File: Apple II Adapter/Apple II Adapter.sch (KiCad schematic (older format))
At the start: 20 parts, among them J1 IDC_PORT1, J2 IDC_PORT2, U1 74HCT04, U2 4066

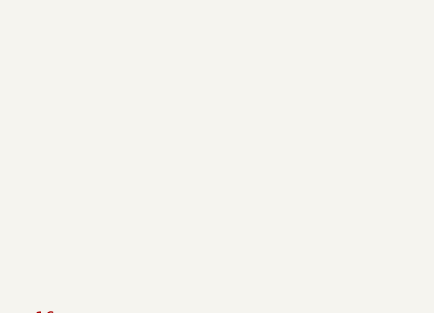
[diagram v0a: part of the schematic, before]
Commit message: Assigned footprints
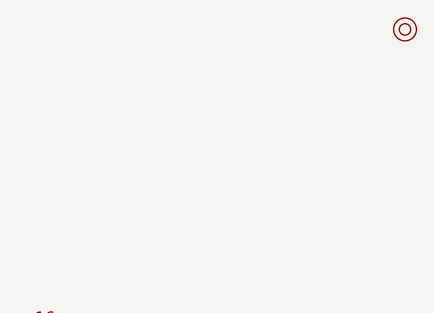
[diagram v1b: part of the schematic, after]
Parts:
- added M1: Mounting, Mounting:M3, symbol mounting:Mounting
- A1: footprint (none) -> Package_DIP:DIP-16_W7.62mm_Socket_LongPads
- C1: footprint (none) -> Capacitor_THT:CP_Radial_D4.0mm_P2.00mm
- J1, J2: footprint (none) -> C64 JoyKEY:IDC_Joystick
- R1, R10, R11, R12, R13, R14, R2, R3, R4, R5, R6, R7, R8, R9: footprint (none) -> Resistor_THT:R_Axial_DIN0207_L6.3mm_D2.5mm_P10.16mm_Horizontal
- U1, U2: footprint (none) -> Package_DIP:DIP-14_W7.62mm_Socket_LongPads
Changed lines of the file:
@@
 F 0 "J1" H 5187 5365 50  0000 C CNN
 F 1 "IDC_PORT1" H 5187 5274 50  0000 C CNN
-F 2 "" H 5200 4625 50  0001 C CNN
+F 2 "C64 JoyKEY:IDC_Joystick" H 5200 4625 50  0001 C CNN
 F 3 "" H 5200 4625 50  0001 C CNN
 	1    5175 4950
@@
 F 0 "J2" H 5187 2565 50  0000 C CNN
 F 1 "IDC_PORT2" H 5187 2474 50  0000 C CNN
-F 2 "" H 5200 1825 50  0001 C CNN
+F 2 "C64 JoyKEY:IDC_Joystick" H 5200 1825 50  0001 C CNN
 F 3 "" H 5200 1825 50  0001 C CNN
 	1    5175 2150
@@
 F 0 "A1" H 9187 2465 50  0000 C CNN
 F 1 "Game_IO" H 9187 2374 50  0000 C CNN
-F 2 "" H 9200 1725 50  0001 C CNN
+F 2 "Package_DIP:DIP-16_W7.62mm_Socket_LongPads" H 9200 1725 50  0001 C CNN
 F 3 "" H 9200 1725 50  0001 C CNN
 	1    9175 2050
@@
 F 0 "U2" H 1700 5527 50  0000 C CNN
 F 1 "4066" H 1700 5436 50  0000 C CNN
-F 2 "" H 1700 5700 50  0001 C CNN
+F 2 "Package_DIP:DIP-14_W7.62mm_Socket_LongPads" H 1700 5700 50  0001 C CNN
 F 3 "http://www.ti.com/lit/ds/symlink/cd4066b.pdf" H 1700 5700 50  0001 C CNN
 	1    1700 5700
@@
 F 0 "U2" H 1700 6777 50  0000 C CNN
 F 1 "4066" H 1700 6686 50  0000 C CNN
-F 2 "" H 1700 6950 50  0001 C CNN
+F 2 "Package_DIP:DIP-14_W7.62mm_Socket_LongPads" H 1700 6950 50  0001 C CNN
 F 3 "http://www.ti.com/lit/ds/symlink/cd4066b.pdf" H 1700 6950 50  0001 C CNN
 	2    1700 6950
@@
 F 0 "U2" H 1700 2727 50  0000 C CNN
 F 1 "4066" H 1700 2636 50  0000 C CNN
-F 2 "" H 1700 2900 50  0001 C CNN
+F 2 "Package_DIP:DIP-14_W7.62mm_Socket_LongPads" H 1700 2900 50  0001 C CNN
 F 3 "http://www.ti.com/lit/ds/symlink/cd4066b.pdf" H 1700 2900 50  0001 C CNN
 	3    1700 2900
@@
 F 0 "U2" H 1700 3977 50  0000 C CNN
 F 1 "4066" H 1700 3886 50  0000 C CNN
-F 2 "" H 1700 4150 50  0001 C CNN
+F 2 "Package_DIP:DIP-14_W7.62mm_Socket_LongPads" H 1700 4150 50  0001 C CNN
 F 3 "http://www.ti.com/lit/ds/symlink/cd4066b.pdf" H 1700 4150 50  0001 C CNN
 	4    1700 4150
@@
 F 0 "U2" H 10580 5696 50  0000 L CNN
 F 1 "4066" H 10580 5605 50  0000 L CNN
-F 2 "" H 10350 5650 50  0001 C CNN
+F 2 "Package_DIP:DIP-14_W7.62mm_Socket_LongPads" H 10350 5650 50  0001 C CNN
 F 3 "http://www.ti.com/lit/ds/symlink/cd4066b.pdf" H 10350 5650 50  0001 C CNN
 	5    10350 5650
@@
 F 0 "U1" H 1325 6892 50  0000 C CNN
 F 1 "74HCT04" H 1325 6801 50  0000 C CNN
-F 2 "" H 1325 6575 50  0001 C CNN
+F 2 "Package_DIP:DIP-14_W7.62mm_Socket_LongPads" H 1325 6575 50  0001 C CNN
 F 3 "https://assets.nexperia.com/documents/data-sheet/74HC_HCT04.pdf" H 1325 6575 50  0001 C CNN
 	1    1325 6575
@@
 F 0 "U1" H 1325 5642 50  0000 C CNN
 F 1 "74HCT04" H 1325 5551 50  0000 C CNN
-F 2 "" H 1325 5325 50  0001 C CNN
+F 2 "Package_DIP:DIP-14_W7.62mm_Socket_LongPads" H 1325 5325 50  0001 C CNN
 F 3 "https://assets.nexperia.com/documents/data-sheet/74HC_HCT04.pdf" H 1325 5325 50  0001 C CNN
 	2    1325 5325
@@
 F 0 "U1" H 7825 6167 50  0000 C CNN
 F 1 "74HCT04" H 7825 6076 50  0000 C CNN
-F 2 "" H 7825 5850 50  0001 C CNN
+F 2 "Package_DIP:DIP-14_W7.62mm_Socket_LongPads" H 7825 5850 50  0001 C CNN
 F 3 "https://assets.nexperia.com/documents/data-sheet/74HC_HCT04.pdf" H 7825 5850 50  0001 C CNN
 	3    7825 5850
@@
 F 0 "U1" H 8325 6167 50  0000 C CNN
 F 1 "74HCT04" H 8325 6076 50  0000 C CNN
-F 2 "" H 8325 5850 50  0001 C CNN
+F 2 "Package_DIP:DIP-14_W7.62mm_Socket_LongPads" H 8325 5850 50  0001 C CNN
 F 3 "https://assets.nexperia.com/documents/data-sheet/74HC_HCT04.pdf" H 8325 5850 50  0001 C CNN
 	4    8325 5850
@@
 F 0 "U1" H 1325 4092 50  0000 C CNN
 F 1 "74HCT04" H 1325 4001 50  0000 C CNN
-F 2 "" H 1325 3775 50  0001 C CNN
+F 2 "Package_DIP:DIP-14_W7.62mm_Socket_LongPads" H 1325 3775 50  0001 C CNN
 F 3 "https://assets.nexperia.com/documents/data-sheet/74HC_HCT04.pdf" H 1325 3775 50  0001 C CNN
 	5    1325 3775
@@
 F 0 "U1" H 1325 2842 50  0000 C CNN
 F 1 "74HCT04" H 1325 2751 50  0000 C CNN
-F 2 "" H 1325 2525 50  0001 C CNN
+F 2 "Package_DIP:DIP-14_W7.62mm_Socket_LongPads" H 1325 2525 50  0001 C CNN
 F 3 "https://assets.nexperia.com/documents/data-sheet/74HC_HCT04.pdf" H 1325 2525 50  0001 C CNN
 	6    1325 2525
@@
 F 0 "U1" H 9730 5696 50  0000 L CNN
 F 1 "74HCT04" H 9730 5605 50  0000 L CNN
-F 2 "" H 9500 5650 50  0001 C CNN
+F 2 "Package_DIP:DIP-14_W7.62mm_Socket_LongPads" H 9500 5650 50  0001 C CNN
 F 3 "https://assets.nexperia.com/documents/data-sheet/74HC_HCT04.pdf" H 9500 5650 50  0001 C CNN
 	7    9500 5650
@@
 F 0 "R11" V 2200 5700 50  0000 C CNN
 F 1 "100k" V 2300 5700 50  0000 C CNN
-F 2 "" V 2230 5700 50  0001 C CNN
+F 2 "Resistor_THT:R_Axial_DIN0207_L6.3mm_D2.5mm_P10.16mm_Horizontal" V 2230 5700 50  0001 C CNN
 F 3 "~" H 2300 5700 50  0001 C CNN
 	1    2300 5700
@@
 F 0 "R12" V 2200 6950 50  0000 C CNN
 F 1 "100k" V 2300 6950 50  0000 C CNN
-F 2 "" V 2230 6950 50  0001 C CNN
+F 2 "Resistor_THT:R_Axial_DIN0207_L6.3mm_D2.5mm_P10.16mm_Horizontal" V 2230 6950 50  0001 C CNN
 F 3 "~" H 2300 6950 50  0001 C CNN
 	1    2300 6950
@@
 F 0 "R14" V 2225 2900 50  0000 C CNN
 F 1 "100k" V 2300 2900 50  0000 C CNN
-F 2 "" V 2230 2900 50  0001 C CNN
+F 2 "Resistor_THT:R_Axial_DIN0207_L6.3mm_D2.5mm_P10.16mm_Horizontal" V 2230 2900 50  0001 C CNN
 F 3 "~" H 2300 2900 50  0001 C CNN
 	1    2300 2900
@@
 F 0 "R10" V 1975 2475 50  0000 C CNN
 F 1 "68k" V 2075 2475 50  0000 C CNN
-F 2 "" V 2005 2475 50  0001 C CNN
+F 2 "Resistor_THT:R_Axial_DIN0207_L6.3mm_D2.5mm_P10.16mm_Horizontal" V 2005 2475 50  0001 C CNN
 F 3 "~" H 2075 2475 50  0001 C CNN
 	1    2075 2475
@@
 F 0 "R13" V 2225 4150 50  0000 C CNN
 F 1 "100k" V 2300 4150 50  0000 C CNN
-F 2 "" V 2230 4150 50  0001 C CNN
+F 2 "Resistor_THT:R_Axial_DIN0207_L6.3mm_D2.5mm_P10.16mm_Horizontal" V 2230 4150 50  0001 C CNN
 F 3 "~" H 2300 4150 50  0001 C CNN
 	1    2300 4150
@@
 F 0 "R9" V 1975 3725 50  0000 C CNN
 F 1 "68k" V 2075 3725 50  0000 C CNN
-F 2 "" V 2005 3725 50  0001 C CNN
+F 2 "Resistor_THT:R_Axial_DIN0207_L6.3mm_D2.5mm_P10.16mm_Horizontal" V 2005 3725 50  0001 C CNN
 F 3 "~" H 2075 3725 50  0001 C CNN
 	1    2075 3725
@@
 F 0 "R7" V 1975 6525 50  0000 C CNN
 F 1 "68k" V 2075 6525 50  0000 C CNN
-F 2 "" V 2005 6525 50  0001 C CNN
+F 2 "Resistor_THT:R_Axial_DIN0207_L6.3mm_D2.5mm_P10.16mm_Horizontal" V 2005 6525 50  0001 C CNN
 F 3 "~" H 2075 6525 50  0001 C CNN
 	1    2075 6525
@@
 F 0 "R8" V 1975 5275 50  0000 C CNN
 F 1 "68k" V 2075 5275 50  0000 C CNN
-F 2 "" V 2005 5275 50  0001 C CNN
+F 2 "Resistor_THT:R_Axial_DIN0207_L6.3mm_D2.5mm_P10.16mm_Horizontal" V 2005 5275 50  0001 C CNN
 F 3 "~" H 2075 5275 50  0001 C CNN
 	1    2075 5275
@@
 F 0 "R2" V 6150 2175 50  0000 C CNN
 F 1 "1k" V 6250 2175 50  0000 C CNN
-F 2 "" V 6180 2175 50  0001 C CNN
+F 2 "Resistor_THT:R_Axial_DIN0207_L6.3mm_D2.5mm_P10.16mm_Horizontal" V 6180 2175 50  0001 C CNN
 F 3 "~" H 6250 2175 50  0001 C CNN
 	1    6250 2175
@@
 F 0 "R1" V 6150 4975 50  0000 C CNN
 F 1 "1k" V 6250 4975 50  0000 C CNN
-F 2 "" V 6180 4975 50  0001 C CNN
+F 2 "Resistor_THT:R_Axial_DIN0207_L6.3mm_D2.5mm_P10.16mm_Horizontal" V 6180 4975 50  0001 C CNN
 F 3 "~" H 6250 4975 50  0001 C CNN
 	1    6250 4975
@@
 F 0 "R3" V 850 6800 50  0000 C CNN
 F 1 "1k" V 950 6800 50  0000 C CNN
-F 2 "" V 880 6800 50  0001 C CNN
+F 2 "Resistor_THT:R_Axial_DIN0207_L6.3mm_D2.5mm_P10.16mm_Horizontal" V 880 6800 50  0001 C CNN
 F 3 "~" H 950 6800 50  0001 C CNN
 	1    950  6800
@@
 F 0 "R4" V 850 5550 50  0000 C CNN
 F 1 "1k" V 950 5550 50  0000 C CNN
-F 2 "" V 880 5550 50  0001 C CNN
+F 2 "Resistor_THT:R_Axial_DIN0207_L6.3mm_D2.5mm_P10.16mm_Horizontal" V 880 5550 50  0001 C CNN
 F 3 "~" H 950 5550 50  0001 C CNN
 	1    950  5550
@@
 F 0 "R5" V 850 2750 50  0000 C CNN
 F 1 "1k" V 950 2750 50  0000 C CNN
-F 2 "" V 880 2750 50  0001 C CNN
+F 2 "Resistor_THT:R_Axial_DIN0207_L6.3mm_D2.5mm_P10.16mm_Horizontal" V 880 2750 50  0001 C CNN
 F 3 "~" H 950 2750 50  0001 C CNN
 	1    950  2750
@@
 F 0 "R6" V 850 4000 50  0000 C CNN
 F 1 "1k" V 950 4000 50  0000 C CNN
-F 2 "" V 880 4000 50  0001 C CNN
+F 2 "Resistor_THT:R_Axial_DIN0207_L6.3mm_D2.5mm_P10.16mm_Horizontal" V 880 4000 50  0001 C CNN
 F 3 "~" H 950 4000 50  0001 C CNN
 	1    950  4000
@@
 F 0 "C1" H 8938 5696 50  0000 L CNN
 F 1 "4.7uF" H 8938 5605 50  0000 L CNN
-F 2 "" H 8850 5650 50  0001 C CNN
+F 2 "Capacitor_THT:CP_Radial_D4.0mm_P2.00mm" H 8850 5650 50  0001 C CNN
 F 3 "~" H 8850 5650 50  0001 C CNN
 	1    8850 5650
@@
 Wire Wire Line
 	6250 4750 7000 4750
+$Comp
+L mounting:Mounting M1
+U 1 1 60630E58
+P 11150 550
+F 0 "M1" H 11150 650 50  0001 C CNN
+F 1 "Mounting" H 11150 475 50  0001 C CNN
+F 2 "Mounting:M3" H 11150 550 50  0001 C CNN
+F 3 "~" H 11150 550 50  0001 C CNN
+	1    11150 550
+	1    0    0    -1
+$EndComp
 $EndSCHEMATC

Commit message: Layout routed
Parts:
- added C1, C2: 100nF, Capacitor_THT:C_Disc_D4.7mm_W2.5mm_P5.00mm, symbol Device:C_Small
- A1: footprint Package_DIP:DIP-16_W7.62mm_Socket_LongPads -> adapter:DIP-16_W7.62mm_Socket_LongPads
- M1: footprint Mounting:M3 -> Mounting:M3_pin
- R5, R6: footprint Resistor_THT:R_Axial_DIN0207_L6.3mm_D2.5mm_P10.16mm_Horizontal -> Resistor_THT:R_Axial_DIN0207_L6.3mm_D2.5mm_P7.62mm_Horizontal
- U2: value 4066 -> CD4066
- renumbered C1 to C3
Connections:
- net GND: now also C1.2, C2.2
- net P1_DOWN: no longer J1.4 (Pin_4), R4.2, U1.3
- net P1_LEFT: no longer J1.1 (Pin_1), R12.2, R7.1, U2.4
- net VCC: now also C1.1, C2.1
- new net P1_RIGHT: J1.4 (Pin_4), R4.2, U1.3
- new net P1_UP: J1.1 (Pin_1), R12.2, R7.1, U2.4
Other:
- moved on the sheet: A1, C3, J1, J2, R1, R10, R11, R12, R13, R14, R2, R3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
